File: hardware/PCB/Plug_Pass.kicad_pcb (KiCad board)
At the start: 2 copper layers, 9 parts, among them J1 Conn_01x06, J10 TDPT-1017503, J2 Conn_01x08, J3 Conn_01x06, J7 Conn_01x06

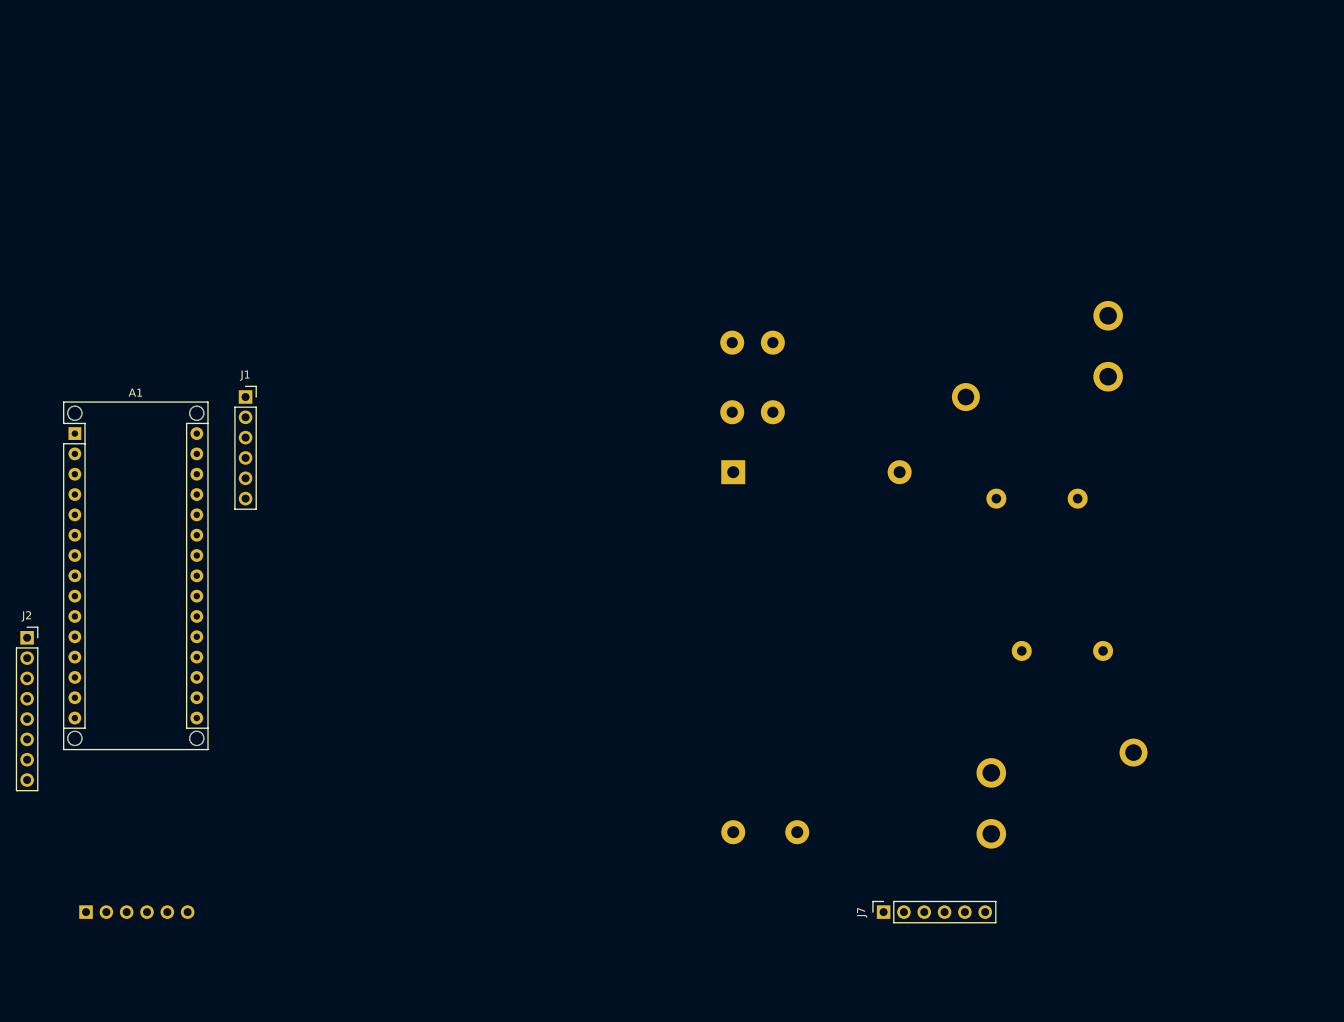
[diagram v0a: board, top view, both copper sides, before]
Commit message: Version 1 of a full PCB design
This push has a full KiCAD package for a set of boards.  Still in draft, but it's complete.
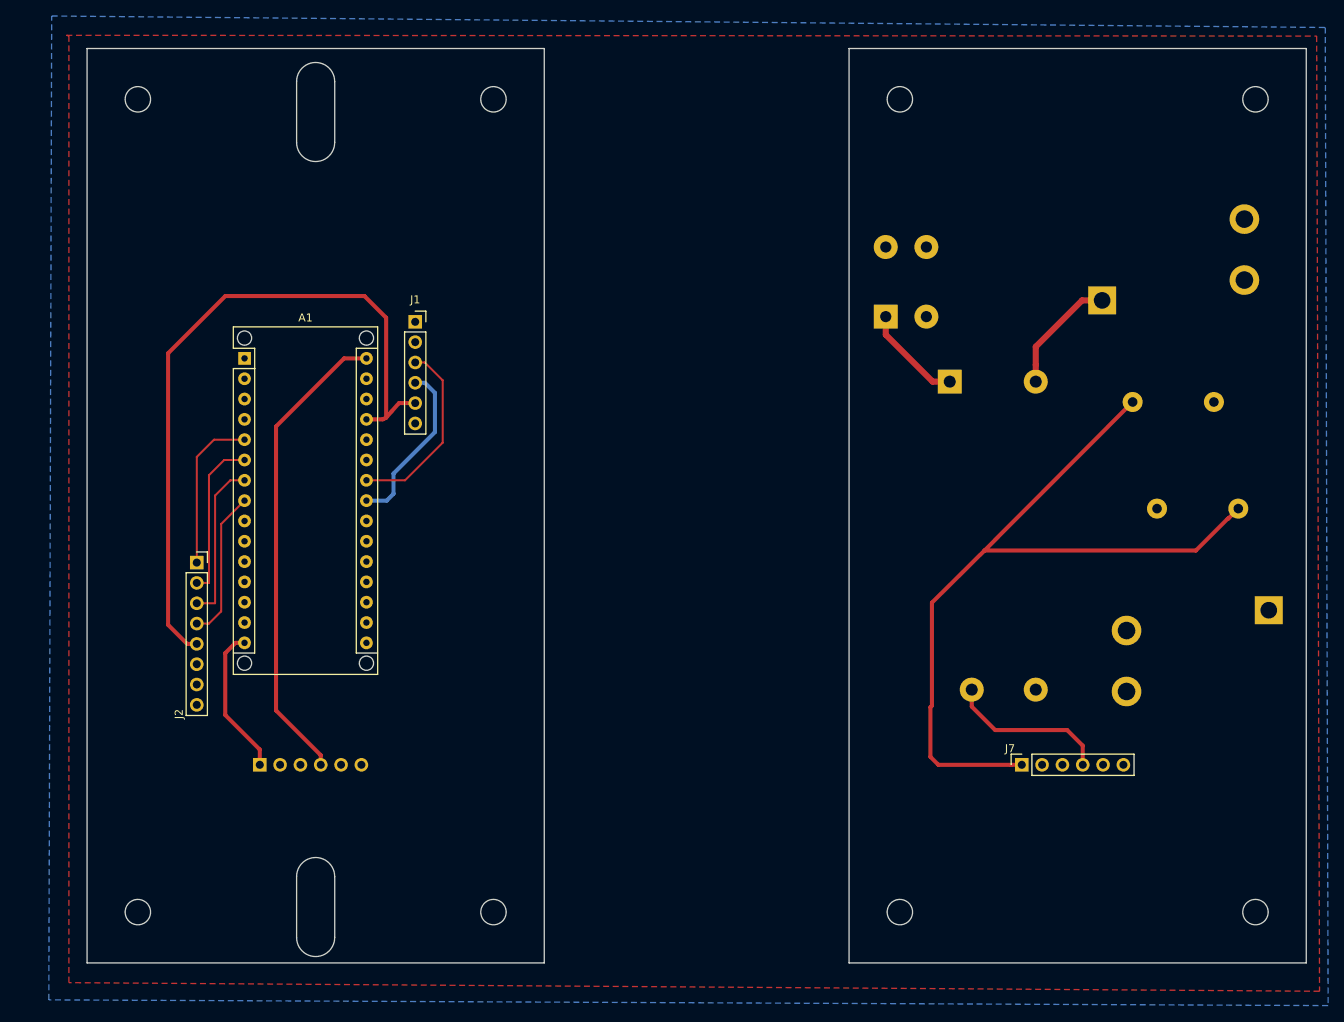
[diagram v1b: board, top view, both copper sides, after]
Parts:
- PS1: value IRM-15-5 -> IRM-05-5; footprint Plug_Pass:Converter_ACDC_MeanWell_IRM-15-5_THT -> Plug_Pass:Converter_ACDC_MeanWell_IRM-05-xx_THT
- moved PS1 29.3 mm to (184.0, 79.7)
- moved J3 28.5 mm to (97.8, 127.6)
- moved J7 25.2 mm to (193.0, 127.6)
- moved RLY2 24.5 mm to (199.8, 122.0)
- moved J2 23.2 mm to (89.9, 102.4)
- moved A1 23.2 mm to (95.9, 76.8)
- moved J1 23.2 mm to (117.2, 72.3)
- moved J10 22.6 mm to (176.0, 71.6)
- moved RLY1 20.9 mm to (227.2, 55.9)
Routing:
- net +5V: track 0.00 -> 169.2 mm
- net /RelayPin: track 0.00 -> 119.2 mm
- net /SCL: track 0.00 -> 23.6 mm
- net /SDA: track 0.00 -> 21.5 mm
- net /MISO: track 0.00 -> 20.2 mm
- net /MOSI: track 0.00 -> 20.2 mm
- net /SCK: track 0.00 -> 20.1 mm
- net /SS: track 0.00 -> 18.7 mm
- net Net-(J9-Pad~): track 0.00 -> 15.1 mm
- net Net-(J10-Pad1): track 0.00 -> 12.7 mm
- added copper zone on B.Cu, net GNDREF
- added copper zone on F.Cu, net GNDREF
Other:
- board outline added: 152.4 x 114.3 mm

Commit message: Revised KiCAD project
added a 120V schematic and pcb board layout that reduces the footprint so it fits in a normal 120V switch slot.
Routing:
- removed copper zone on B.Cu, net GNDREF
- removed copper zone on F.Cu, net GNDREF
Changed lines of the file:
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@@
   )
   (setup
-    (last_trace_width 0.508)
+    (last_trace_width 0.254)
     (user_trace_width 0.508)
     (user_trace_width 0.762)
@@
   (segment (start 194.7857 77.61944) (end 194.7857 79.74076) (width 0.762) (layer F.Cu) (net 46))
   (segment (start 203.0857 69.58476) (end 200.5737 69.58476) (width 0.762) (layer F.Cu) (net 46))
-  (zone (net 7) (net_name GNDREF) (layer F.Cu) (hatch edge 0.508)
-    (connect_pads (clearance 0.508))
-    (min_thickness 0.254)
-    (fill yes (arc_segments 32) (thermal_gap 0.508) (thermal_bridge_width 0.508))
-    (polygon
-      (pts
-        (xy 229.90048 36.54552) (xy 230.25862 155.9433) (xy 73.92924 154.86888) (xy 73.92924 36.54552) (xy 73.61428 36.449)
-      )
-    )
-  )
-  (zone (net 7) (net_name GNDREF) (layer B.Cu) (hatch edge 0.508)
-    (connect_pads (clearance 0.508))
-    (min_thickness 0.254)
-    (fill yes (arc_segments 32) (thermal_gap 0.508) (thermal_bridge_width 0.508))
-    (polygon
-      (pts
-        (xy 230.9749 35.4711) (xy 231.33304 157.73654) (xy 71.41972 157.02026) (xy 71.77786 34.036)
-      )
-    )
-  )
 )

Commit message: Add files via upload
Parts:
- removed J7: Conn_01x06, Plug_Pass:PinSocket_1x06_P2.54mm_Vertical
- added J4: Conn_02x04_Odd_Even, Plug_Pass:IDC-Header_2x04_P2.54mm_Vertical, B.Cu at (211.4, 95.0)
- J10: footprint Plug_Pass:TDPT_2P_5.08MM -> Plug_Pass:TDPT_2P_6.35MM
- J3: value Conn_01x06 -> Conn_02x04_Odd_Even; footprint Plug_Pass:PinHeader_1x06_P2.54mm_Vertical -> Plug_Pass:IDC-Header_2x04_P2.54mm_Vertical
- RLY2: value T95S5D22-5 -> G5V-1-DC5; footprint Plug_Pass:RLY-T9AS5D22-5 -> Plug_Pass:Relay_THT_G5V-1
- moved RLY2 98.0 mm to (102.2, 113.9), turned to 90 degrees
- moved RLY1 68.6 mm to (181.8, 107.3), turned to 270 degrees
- moved J3 33.1 mm to (103.4, 95.0), turned to 0 degrees
- moved J10 32.7 mm to (208.3, 77.2)
- moved PS1 23.3 mm to (192.8, 101.4), turned to 90 degrees
- moved J2 17.8 mm to (89.5, 120.2), turned to 180 degrees
- moved J1 3.27 mm to (120.5, 72.3)
- moved A1 1.27 mm to (97.2, 76.8)
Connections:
- A1 pad 15: /RelayPin -> Net-(A1-Pad15)
- A1 pad 30: +5V -> VCC
- J10 pad 2: Net-(J10-Pad2) -> GNDREF
- J3 pad 4: +5V -> Net-(J3-Pad4)
- J3 pad 5: Net-(J3-Pad5) -> VCC
- J3 pad 6: GNDREF -> Net-(J3-Pad6)
- PS1 pad 4: +5V -> VCC
- RLY2 pad 2: GNDREF -> Net-(A1-Pad15)
- RLY2 pad 5: /RelayPin -> VCC
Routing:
- net +5V: track 169.2 -> 71.2 mm
- net /RelayPin: track 119.2 -> 42.9 mm
- net VCC: track 0.00 -> 76.1 mm
- net /SCK: track 20.1 -> 41.5 mm
- net Net-(J10-Pad1): track 12.7 -> 32.0 mm
- net /MISO: track 20.2 -> 35.0 mm
- net /MOSI: track 20.2 -> 26.9 mm
- net Net-(A1-Pad15): track 0.00 -> 5.45 mm
- net /SS: track 18.7 -> 22.7 mm
- net Net-(J9-Pad~): track 15.1 -> 18.6 mm
- net /SCL: track 23.6 -> 24.3 mm
- net /SDA: track 21.5 -> 20.9 mm
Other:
- board size 152.4 x 114.3 mm -> 134.6 x 108 mm
- board text added: "Clatskanie People's Utility District"
- board text added: "Plug Pass version 1.0 120V Outlet RFID control module"

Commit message: Add files via upload
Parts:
- J3: moved to F.Cu
- moved RLY2 109.2 mm to (206.5, 81.8), turned to 0 degrees
- moved A1 21.7 mm to (86.4, 95.7), turned to 90 degrees
- moved J3 20.2 mm to (121.9, 103.1)
- moved J2 18.8 mm to (97.9, 103.3), turned to 90 degrees
- moved J1 11.0 mm to (120.5, 61.3)
- moved J4 2.28 mm to (213.6, 94.5), turned to 180 degrees
- moved RLY1 1.00 mm to (181.8, 108.3)
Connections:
- A1 pad 15: Net-(A1-Pad15) -> /RLY2-Pin
- J3 pad 1: /RelayPin -> /RLY2-Pin
- J4 pad 1: /RelayPin -> /RLY2-Pin
- RLY1 pad 5: /RelayPin -> /RLY1-Pin
- RLY2 pad 10: /RelayPin -> /RLY1-Pin
- RLY2 pad 2: Net-(A1-Pad15) -> /RLY2-Pin
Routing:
- net VCC: track 76.1 -> 126.9 mm
- net /RelayPin: track 42.9 -> 0.00 mm
- net /SCK: track 41.5 -> 8.19 mm
- net /RLY1-Pin: track 0.00 -> 29.2 mm
- net /MISO: track 35.0 -> 8.19 mm
- net /RLY2-Pin: track 0.00 -> 22.9 mm
- net /MOSI: track 26.9 -> 8.19 mm
- net /SS: track 22.7 -> 8.19 mm
- net +5V: track 71.2 -> 84.1 mm
- net Net-(A1-Pad15): track 5.45 -> 0.00 mm
- net /SCL: track 24.3 -> 28.1 mm
- net /SDA: track 20.9 -> 24.2 mm
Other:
- board size 134.6 x 108 mm -> 139.7 x 108 mm
- board text added: "Plug Pass version 1.2 120V RFID control module"
- board text added: "Plug Pass version 1.2 AC shield"
- board text added: "Plug Pass version 1.2 arduino shield"
- board text removed: "Plug Pass version 1.0 120V Outlet RFID control module"

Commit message: Add files via upload
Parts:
- removed J10: TDPT-1017503, Plug_Pass:TDPT_2P_6.35MM
- added H1: MountingHole_Pad, Plug_Pass:Ground_Pad, F.Cu at (176.3, 62.5)
- added H2: MountingHole_Pad, Plug_Pass:Ground_Pad, F.Cu at (176.3, 129.5)
- added H3: MountingHole_Pad, Plug_Pass:Ground_Pad, F.Cu at (217.9, 62.5)
- added H4: MountingHole_Pad, Plug_Pass:Ground_Pad, F.Cu at (217.9, 129.5)
- added J6: Screw_Terminal_01x01, Plug_Pass:PLH5-1_75, B.Cu at (187.5, 125.5)
- A1: value Arduino_Nano_v3.x -> Arduino_Nano_Every; footprint Plug_Pass:Arduino_Nano_WithMountingHoles -> Plug_Pass:NANO_33_Footprint_SMD_Castell
- J1: footprint Plug_Pass:PinSocket_1x06_P2.54mm_Vertical -> Plug_Pass:RTC_PinHeader
- J2: footprint Plug_Pass:PinSocket_1x08_P2.54mm_Vertical -> Plug_Pass:PN532_NFC_PinSocket
- J3: footprint Plug_Pass:IDC-Header_2x04_P2.54mm_Vertical -> Plug_Pass:IDC-Header_2x04_P2.54mm_Vertical_Small
- moved RLY2 32.2 mm to (216.9, 112.3), turned to 270 degrees
- moved A1 27.2 mm to (104.1, 116.3), turned to 0 degrees
- moved PS1 25.5 mm to (177.8, 80.8), turned to 0 degrees
- moved RLY1 16.5 mm to (175.8, 93.0)
- moved J2 10.4 mm to (97.5, 93.0)
- moved J3 9.86 mm to (119.9, 93.5)
- moved J1 7.88 mm to (121.4, 69.1)
- moved J4 3.98 mm to (215.4, 98.0)
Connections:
- J3 pad 2: Net-(J3-Pad2) -> GNDREF
- J3 pad 4: Net-(J3-Pad4) -> GNDREF
- J3 pad 6: Net-(J3-Pad6) -> GNDREF
- J3 pad 8: Net-(J3-Pad8) -> GNDREF
- J4 pad 2: Net-(J4-Pad2) -> GNDREF
- J4 pad 4: Net-(J4-Pad4) -> GNDREF
- J4 pad 6: Net-(J4-Pad6) -> GNDREF
- J4 pad 8: Net-(J4-Pad8) -> GNDREF
- PS1 pad 1: Net-(J10-Pad1) -> NEUT
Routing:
- net NEUT: track 0.00 -> 61.2 mm
- net /RLY2-Pin: track 22.9 -> 56.0 mm, vias 0 -> 1
- net VCC: track 126.9 -> 94.9 mm
- net Net-(J10-Pad1): track 32.0 -> 0.00 mm
- net /SDA: track 24.2 -> 54.9 mm, vias 0 -> 1
- net +5V: track 84.1 -> 54.0 mm, vias 0 -> 1
- net /SCL: track 28.1 -> 56.0 mm
- net /SS: track 8.19 -> 32.0 mm, vias 0 -> 1
- net /SCK: track 8.19 -> 32.0 mm, vias 0 -> 1
- net /MOSI: track 8.19 -> 32.0 mm, vias 0 -> 1
- net /MISO: track 8.19 -> 32.0 mm, vias 0 -> 1
- net Net-(J9-Pad~): track 18.8 -> 33.7 mm
- net /RLY1-Pin: track 29.2 -> 19.0 mm
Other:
- board size 139.7 x 108 mm -> 140.7 x 73.2 mm
- board text added: "Clatskanie People's Utility District Plug Pass - 120V RFID control module v2.0"
- board text added: "Clatskanie People's Utility District Plug Pass - v2.0 - AC shield"
- board text added: "Clatskanie People's Utility District Plug Pass - v2.0 - arduino shield"
- board text added: "GND"
- board text removed: "Clatskanie People's Utility District"
- board text removed: "Plug Pass version 1.2 120V RFID control module"
- board text removed: "Plug Pass version 1.2 AC shield"
- board text removed: "Plug Pass version 1.2 arduino shield"

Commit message: Add files via upload
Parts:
- removed J3: Conn_02x04_Odd_Even, Plug_Pass:IDC-Header_2x04_P2.54mm_Vertical_Small
- removed J4: Conn_02x04_Odd_Even, Plug_Pass:IDC-Header_2x04_P2.54mm_Vertical
- moved RLY2 58.9 mm to (158.5, 119.9), turned to 0 degrees
- moved RLY1 56.4 mm to (135.6, 53.3)
- moved A1 49.4 mm to (152.9, 108.2)
- moved J1 49.1 mm to (170.2, 63.0)
- moved J2 49.1 mm to (146.3, 86.9)
- moved PS1 46.4 mm to (133.6, 95.0)
- moved J6 45.3 mm to (142.2, 122.2)
- moved H1 44.6 mm to (132.1, 56.4)
- moved H2 44.6 mm to (132.1, 123.4)
- moved H3 44.6 mm to (173.7, 56.4)
- moved H4 44.6 mm to (173.7, 123.4)
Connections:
- net Net-(J9-Pad~) renamed /AC-L
- A1 pad 11: Net-(A1-Pad11) -> /SS
- A1 pad 14: Net-(A1-Pad14) -> /MOSI
- A1 pad 15: /RLY2-Pin -> /MISO
- A1 pad 16: Net-(A1-Pad16) -> /SCK
- A1 pad 5: /SCK -> /RLY2-Pin
- A1 pad 6: /MISO -> Net-(A1-Pad6)
- A1 pad 7: /MOSI -> Net-(A1-Pad7)
- A1 pad 8: /SS -> Net-(A1-Pad8)
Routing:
- net /RLY1-Pin: track 19.0 -> 80.9 mm
- net /RLY2-Pin: track 56.0 -> 20.6 mm, vias 1 -> 0
- net VCC: track 94.9 -> 75.5 mm
- net NEUT: track 61.2 -> 44.6 mm
- net /MISO: track 32.0 -> 47.3 mm, vias 1 -> 2
- net /MOSI: track 32.0 -> 45.6 mm, vias 1 -> 2
- net /SCL: track 56.0 -> 65.9 mm
- net /SCK: track 32.0 -> 37.7 mm, vias 1 -> 2
- net /SDA: track 54.9 -> 59.5 mm, vias 1 -> 0
- net +5V: track 54.0 -> 50.3 mm, vias 1 -> 2
- net /AC-L: track 33.7 -> 35.5 mm
- net /SS: track 32.0 -> 33.0 mm, vias 1 -> 2
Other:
- board size 140.7 x 73.2 mm -> 47.8 x 73.2 mm
- board text added: "Clatskanie People's Utility District Plug Pass - 120V RFID control module v2.2"
- board text removed: "Clatskanie People's Utility District Plug Pass - 120V RFID control module v2.0"
- board text removed: "Clatskanie People's Utility District Plug Pass - v2.0 - AC shield"
- board text removed: "Clatskanie People's Utility District Plug Pass - v2.0 - arduino shield"

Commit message: Add files via upload
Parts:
- removed A1: Arduino_Nano_Every, Plug_Pass:NANO_33_Footprint_SMD_Castell
- removed H1, H2, H3, H4: MountingHole_Pad, Plug_Pass:Ground_Pad
- removed J6: Screw_Terminal_01x01, Plug_Pass:PLH5-1_75
- added B1: CR1220, Plug_Pass:CR1220, F.Cu at (142.7, 62.0)
- added C1: 0.1µF, Plug_Pass:0603-1608X90N, F.Cu at (137.4, 87.4)
- added C10: 100pF, Plug_Pass:0603-1608X90N, F.Cu at (142.2, 110.9)
- added C11: 220pF, Plug_Pass:0402-1005X55N, F.Cu at (141.6, 104.8)
- added C12: NC, Plug_Pass:0805-R2013X50N, F.Cu at (150.0, 113.0)
- added C13: 100pF, Plug_Pass:0603-1608X90N, F.Cu at (150.0, 110.9)
- added C14: 220pF, Plug_Pass:0402-1005X55N, F.Cu at (149.2, 104.8)
- added C15: 22pF, Plug_Pass:0402-1005X55N, F.Cu at (150.1, 109.0)
- added C16: NC, Plug_Pass:0805-R2013X50N, F.Cu at (149.9, 106.9)
- added C17: 0.1µF, Plug_Pass:0603-1608X90N, F.Cu at (152.9, 95.0)
- added C18: 0.1µF, Plug_Pass:0603-1608X90N, F.Cu at (145.3, 82.3)
- added C19: 10µF, Plug_Pass:0603-1608X90N, F.Cu at (150.9, 95.0)
- added C2: 0.1µF, Plug_Pass:0603-1608X90N, F.Cu at (134.1, 89.4)
- added C20: 0.1µF, Plug_Pass:0603-1608X90N, F.Cu at (154.2, 90.9)
- added C21: 10µF, Plug_Pass:0603-1608X90N, F.Cu at (155.2, 60.2)
- added C22: 10µF, Plug_Pass:0603-1608X90N, F.Cu at (157.5, 60.2)
- added C23: 1000pF, Plug_Pass:0603-1608X90N, F.Cu at (154.2, 88.9)
- added C24: 33pF, Plug_Pass:0603-1608X90N, F.Cu at (151.9, 85.3)
- added C25: 33pF, Plug_Pass:0603-1608X90N, F.Cu at (151.9, 77.5)
- added C26: 1µF, Plug_Pass:0402-1005X55N, F.Cu at (153.3, 58.0)
- added C27: 4,7uF_16V, Plug_Pass:CAPAE430X550N, F.Cu at (133.1, 68.6)
- added C28: 1µF, Plug_Pass:0402-1005X55N, F.Cu at (151.5, 58.0)
- added C29: 100nF, Plug_Pass:0402-1005X55N, F.Cu at (151.9, 75.9)
- added C3: 0.1µF, Plug_Pass:0603-1608X90N, F.Cu at (156.5, 99.8)
- added C30: 100nF, Plug_Pass:0402-1005X55N, F.Cu at (164.6, 81.5)
- added C31: 4,7uF_16V, Plug_Pass:CAPAE430X550N, F.Cu at (167.4, 109.2)
- added C32: 1uF, Plug_Pass:0402-1005X55N, F.Cu at (171.4, 81.5)
- added C33: 100nF, Plug_Pass:0402-1005X55N, F.Cu at (168.1, 113.3)
- added C4: 10µF, Plug_Pass:0603-1608X90N, F.Cu at (152.4, 99.8)
- added C5: 10µF, Plug_Pass:0603-1608X90N, F.Cu at (138.4, 85.3)
- added C6: 22pF, Plug_Pass:0402-1005X55N, F.Cu at (142.2, 109.0)
- added C7: NC, Plug_Pass:0805-R2013X50N, F.Cu at (142.2, 106.9)
- added C8: 0.1µF, Plug_Pass:0603-1608X90N, F.Cu at (150.4, 99.8)
- added C9: NC, Plug_Pass:0805-R2013X50N, F.Cu at (142.2, 113.0)
- added D1: 0025_SS1P3L-M3_84A, Plug_Pass:DO220AAL, F.Cu at (169.2, 103.9)
- added F1: MFFSMF050, Plug_Pass:0603-1608X90N, F.Cu at (166.1, 113.8)
- added GND: GND, Plug_Pass:Ground_Pad, F.Cu at (135.9, 114.7)
- added GND2: GND, Plug_Pass:Ground_Pad, F.Cu at (132.1, 56.4)
- added GND3: GND, Plug_Pass:Ground_Pad, F.Cu at (132.1, 123.4)
- added GND4: GND, Plug_Pass:Ground_Pad, F.Cu at (173.7, 56.4)
- added GND5: GND, Plug_Pass:Ground_Pad, F.Cu at (173.7, 123.4)
- added IC1: DS3231M, Package_SO:SOIC-16W_7.5x10.3mm_P1.27mm, F.Cu at (166.9, 66.3)
- added IC2: PN532, Plug_Pass:HVQFN40-6X6, F.Cu at (144.0, 88.4)
- added IC3: VREG_SOT23-5, Plug_Pass:SOT23-5, F.Cu at (156.5, 64.3)
- added IC4: FT232RL, digikey-footprints:SSOP-28_W5.30mm, F.Cu at (168.1, 88.1)
- added IC5: ATMEGA328P-AUR, digikey-footprints:TQFP-32_7x7mm, F.Cu at (138.2, 77.5)
- added L1: Yellow, Plug_Pass:LEDC1608X80N-AK, F.Cu at (170.9, 78.2)
- added L2: FERRITE, Plug_Pass:0805-R2013X50N, F.Cu at (154.4, 99.8)
- added L3: 560nH, Plug_Pass:0805-R2013X50N, F.Cu at (141.2, 95.0)
- added L4: 560nH, Plug_Pass:0805-R2013X50N, F.Cu at (146.6, 95.0)
- added L5: FERRITE, Plug_Pass:0805-R2013X50N, F.Cu at (154.9, 95.0)
- added NEUT: NEUT, Plug_Pass:Ground_Pad, F.Cu at (135.9, 107.4)
- added PWR1: Green, Plug_Pass:LEDC1608X80N-AK, F.Cu at (152.1, 72.9)
- added R1: 1.5, Plug_Pass:0402-1005X55N, F.Cu at (145.7, 113.5)
- added R10: 330, Plug_Pass:0402-1005X55N, F.Cu at (167.1, 75.9)
- added R11: 330, Plug_Pass:0402-1005X55N, F.Cu at (167.1, 74.2)
- added R12: 330, Plug_Pass:0402-1005X55N, F.Cu at (167.1, 77.5)
- added R2: 10k, Plug_Pass:0402-1005X55N, F.Cu at (157.7, 69.3)
- added R3: NC, Plug_Pass:R0201, F.Cu at (147.6, 115.7)
- added R4: 10k, Plug_Pass:0402-1005X55N, F.Cu at (155.2, 69.3)
- added R5: NC, Plug_Pass:R0201, F.Cu at (151.3, 115.7)
- added R6: 1.5, Plug_Pass:0402-1005X55N, F.Cu at (153.2, 113.5)
- added R7: 1.0k, Plug_Pass:0402-1005X55N, F.Cu at (151.1, 89.9)
- added R8: 1.69k, Plug_Pass:0402-1005X55N, F.Cu at (157.7, 88.9)
- added R9: 330, Plug_Pass:0402-1005X55N, F.Cu at (148.6, 72.9)
- added RP1: 1k, Plug_Pass:CAY16, F.Cu at (149.1, 69.3)
- added RX1: Red, Plug_Pass:LEDC1608X80N-AK, F.Cu at (170.9, 75.9)
- added SW1: RESET, Plug_Pass:C&K_PTS820_NO_HOLES, F.Cu at (158.5, 84.3)
- added TP1: TX1_POST, Plug_Pass:TESTPOINT_ROUND_1MM, F.Cu at (141.2, 98.0)
- added TP2: TGND, Plug_Pass:TESTPOINT_ROUND_1MM, F.Cu at (144.0, 98.0)
- added TP3: TX2_POST, Plug_Pass:TESTPOINT_ROUND_1MM, F.Cu at (146.6, 98.0)
- added TP4: TX1_PRE, Plug_Pass:TESTPOINT_ROUND_1MM, F.Cu at (145.7, 115.3)
- added TP5: TGND, Plug_Pass:TESTPOINT_ROUND_1MM, F.Cu at (149.4, 115.2)
- added TP6: TX2_PRE, Plug_Pass:TESTPOINT_ROUND_1MM, F.Cu at (153.2, 115.2)
- added TP7: RX, Plug_Pass:TESTPOINT_ROUND_1MM, F.Cu at (161.0, 88.9)
- added TP8: D11, Plug_Pass:TESTPOINT_ROUND_1MM, F.Cu at (172.2, 106.9)
- added TP9: D+1, Plug_Pass:TESTPOINT_ROUND_1MM, F.Cu at (174.2, 106.9)
- added TX1: Green, Plug_Pass:LEDC1608X80N-AK, F.Cu at (170.9, 73.7)
- added Y1: 27.12MHz, Plug_Pass:7M27120MAAJT, F.Cu at (151.9, 81.3)
- added Y2: 16MHz, Plug_Pass:CSTNE16M0V51Z000R0, F.Cu at (133.1, 85.3)
- J1: value Conn_01x06 -> USB_B_Micro; footprint Plug_Pass:RTC_PinHeader -> Plug_Pass:MOLEX_1051330001; moved to B.Cu
- J2: value Conn_01x08 -> 505568-0271; footprint Plug_Pass:PN532_NFC_PinSocket -> Plug_Pass:5055680271
- PS1: value IRM-05-5 -> IRM-03-5; footprint Plug_Pass:Converter_ACDC_MeanWell_IRM-05-xx_THT -> Converter_ACDC:Converter_ACDC_MeanWell_IRM-03-xx_SMD
- RLY1: footprint Plug_Pass:RLY-T9AS5D22-5 -> Plug_Pass:RLY-T9AS1D22-5
- moved RLY1 74.5 mm to (172.5, 118.1), turned to 90 degrees
- moved J1 58.7 mm to (164.5, 121.4), turned to 180 degrees
- moved J2 32.9 mm to (149.4, 119.6), turned to 180 degrees
- moved RLY2 31.0 mm to (133.1, 102.1), turned to 90 degrees
- moved PS1 29.1 mm to (153.9, 74.2), turned to 90 degrees
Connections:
- net /RLY1-Pin renamed /RLY1
- J1 pad 1: /32K -> Net-(F1-Pad1)
- J1 pad 2: /SQW -> /D-
- J1 pad 3: /SCL -> /D+
- J1 pad 4: /SDA -> Net-(J1-Pad4)
- J1 pad 5: +5V -> GNDREF
- J2 pad 1: /SCK -> Net-(J2-Pad1)
- J2 pad 2: /MISO -> Net-(J2-Pad2)
- J2 pad 3: /MOSI -> GNDREF
- J2 pad 4: /SS -> GNDREF
- PS1 pad 1: NEUT -> AC-L
- PS1 pad 3: GNDREF -> /NEUT
- RLY1 pad 1: /AC-L -> AC-L
- RLY2 pad 2: /RLY2-Pin -> RLY2
- RLY2 pad 5: VCC -> +5V
- RLY2 pad 6: VCC -> +5V
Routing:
- net +5V: track 50.3 -> 231.0 mm, vias 2 -> 4
- net GNDREF: track 0.00 -> 99.2 mm, vias 0 -> 14
- net +3V3: track 0.00 -> 96.6 mm, vias 0 -> 5
- net LDO: track 0.00 -> 85.7 mm, vias 0 -> 2
- net VCC: track 75.5 -> 0.00 mm
- net /RLY1: track 80.9 -> 12.2 mm
- net /SCL: track 65.9 -> 0.00 mm
- net /SDA: track 59.5 -> 0.00 mm
- net /MISO: track 47.3 -> 0.00 mm, vias 2 -> 0
- net /MOSI: track 45.6 -> 0.00 mm, vias 2 -> 0
- net NEUT: track 44.6 -> 0.00 mm
- net TX: track 0.00 -> 42.6 mm, vias 0 -> 4
- net /NEUT: track 0.00 -> 42.5 mm
- net SDA: track 0.00 -> 42.3 mm
- net Net-(C14-Pad2): track 0.00 -> 38.2 mm, vias 0 -> 2
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- added copper zone on B.Cu, net GNDREF
- added copper zone on F.Cu, net GNDREF
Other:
- board text added: "Clatskanie People's Utility District Plug Pass - 120V Switch v3.0"
- board text removed: "Clatskanie People's Utility District Plug Pass - 120V RFID control module v2.2"
- board text removed: "GND"
